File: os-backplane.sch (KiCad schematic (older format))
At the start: 64 parts, among them J9 FPANEL

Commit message: Reannotated parts
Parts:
- renumbered C2 to C1, J9 to J1, R3 to R1, R7 to R10, R5 to R11, R6 to R12, R4 to R13, R10 to R14, R11 to R15, R47 to R16, R48 to R17, R50 to R18, R49 to R19, R43 to R2, R51 to R20, R52 to R21, R54 to R22, R53 to R23, R55 to R24, R56 to R25, R58 to R26, R57 to R27, R59 to R28, R60 to R29, R44 to R3, R62 to R30, R61 to R31, R63 to R32, R64 to R33, R66 to R34, R65 to R35, R67 to R36, R68 to R37, R70 to R38, R69 to R39, R45 to R4, R71 to R40, R72 to R41, R74 to R42, R73 to R43, R75 to R44, R76 to R45, R78 to R46, R77 to R47, R79 to R48, R80 to R49, R46 to R5, R82 to R50, R81 to R51, R1 to R6, R2 to R7, R9 to R8, R8 to R9
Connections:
- net +3.3SB: now also R1.2

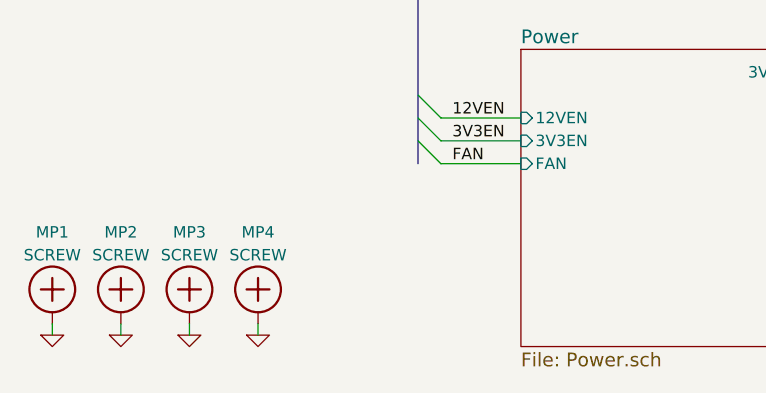
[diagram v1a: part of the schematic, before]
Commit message: Added extra supports
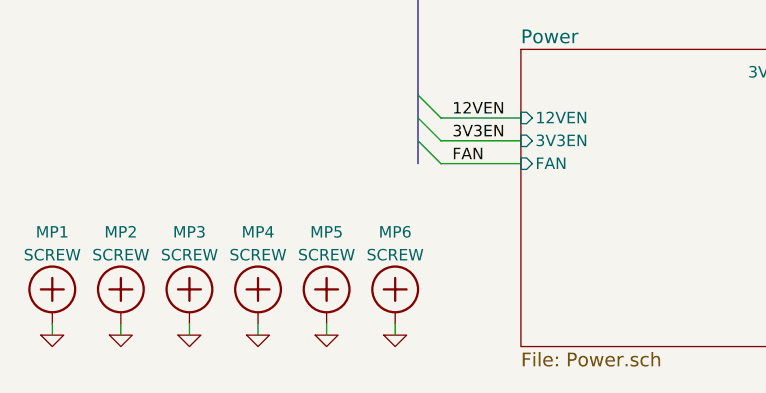
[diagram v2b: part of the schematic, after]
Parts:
- added MP5, MP6: SCREW, mech:SCREW-4-SUPPORTED, symbol SCREW
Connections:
- net GND: now also MP5.1, MP6.1
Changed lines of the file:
@@
 	4900 8750 6200 8750
 Connection ~ 5250 1200
+$Comp
+L SCREW MP5
+U 1 1 54D8065B
+P 2000 10050
+F 0 "MP5" H 2000 10300 50  0000 C CNN
+F 1 "SCREW" H 2000 10200 50  0000 C CNN
+F 2 "mech:SCREW-4-SUPPORTED" H 2000 10050 50  0001 C CNN
+F 3 "" H 2000 10050 60  0000 C CNN
+F 4 "MP3" H 2000 10050 50  0001 C CNN "OldReference"
+	1    2000 10050
+	1    0    0    -1
+$EndComp
+$Comp
+L GND #PWR0206
+U 1 1 54D80662
+P 2000 10250
+F 0 "#PWR0206" H 2000 10250 30  0001 C CNN
+F 1 "GND" H 2000 10180 30  0001 C CNN
+F 2 "" H 2000 10250 60  0000 C CNN
+F 3 "" H 2000 10250 60  0000 C CNN
+F 4 "#PWR0193" H 2000 10250 50  0001 C CNN "OldReference"
+	1    2000 10250
+	1    0    0    -1
+$EndComp
+$Comp
+L SCREW MP6
+U 1 1 54D80669
+P 2300 10050
+F 0 "MP6" H 2300 10300 50  0000 C CNN
+F 1 "SCREW" H 2300 10200 50  0000 C CNN
+F 2 "mech:SCREW-4-SUPPORTED" H 2300 10050 50  0001 C CNN
+F 3 "" H 2300 10050 60  0000 C CNN
+F 4 "MP4" H 2300 10050 50  0001 C CNN "OldReference"
+	1    2300 10050
+	1    0    0    -1
+$EndComp
+$Comp
+L GND #PWR0207
+U 1 1 54D80670
+P 2300 10250
+F 0 "#PWR0207" H 2300 10250 30  0001 C CNN
+F 1 "GND" H 2300 10180 30  0001 C CNN
+F 2 "" H 2300 10250 60  0000 C CNN
+F 3 "" H 2300 10250 60  0000 C CNN
+F 4 "#PWR0194" H 2300 10250 50  0001 C CNN "OldReference"
+	1    2300 10250
+	1    0    0    -1
+$EndComp
+Wire Wire Line
+	2000 10250 2000 10200
+Wire Wire Line
+	2300 10250 2300 10200
 $EndSCHEMATC
